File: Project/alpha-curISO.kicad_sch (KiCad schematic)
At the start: 43 parts, among them J2 SWD, U1 RP2040, U5 74AHCT1G125

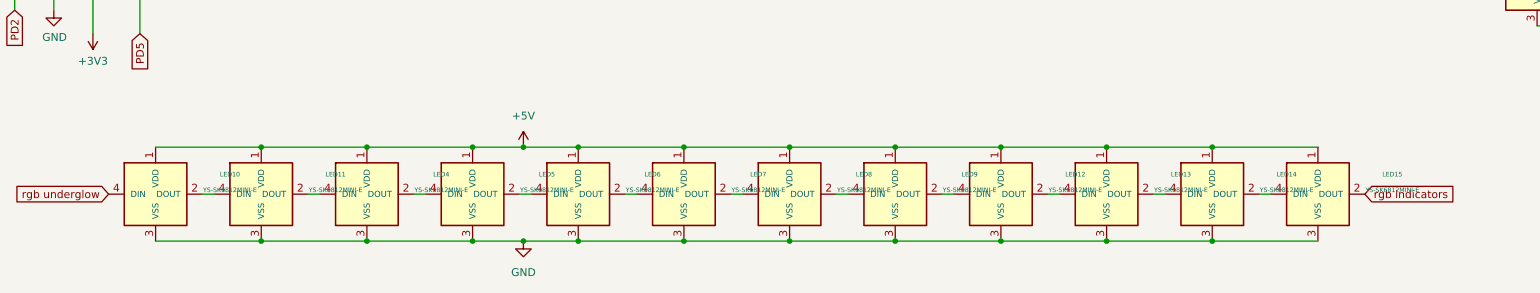
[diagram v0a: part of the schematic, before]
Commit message: added plate project for breakoff
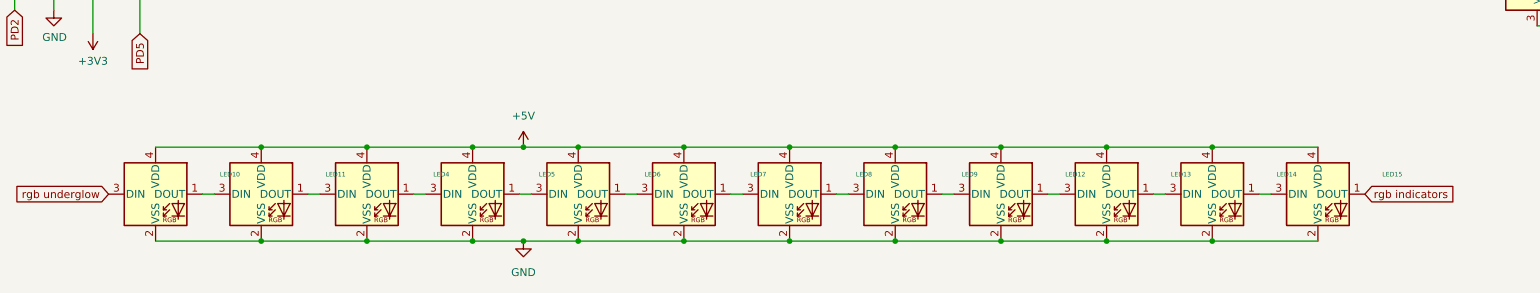
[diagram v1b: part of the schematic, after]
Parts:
- LED10, LED11, LED12, LED13, LED14, LED15, LED4, LED5, LED6, LED7, LED8, LED9: value YS-SK6812MINI-E -> WS2812_2020; footprint CrumpPrints:WS2812-2020 -> PCM_marbastlib-various:LED_WS2812_2020; symbol kbd:YS-SK6812MINI-E -> PCM_marbastlib-various:WS2812_2020
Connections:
- net +5V: now also LED10.4 (VDD), LED11.4 (VDD), LED12.4 (VDD), LED13.4 (VDD), LED14.4 (VDD), LED15.4 (VDD), LED4.4 (VDD), LED5.4 (VDD), LED6.4 (VDD), LED7.4 (VDD), LED8.4 (VDD), LED9.4 (VDD); no longer LED10.1 (VDD), LED11.1 (VDD), LED12.1 (VDD), LED13.1 (VDD), LED14.1 (VDD), LED15.1 (VDD), LED4.1 (VDD), LED5.1 (VDD), LED6.1 (VDD), LED7.1 (VDD), LED8.1 (VDD), LED9.1 (VDD)
- net GND: now also LED10.2 (VSS), LED11.2 (VSS), LED12.2 (VSS), LED13.2 (VSS), LED14.2 (VSS), LED15.2 (VSS), LED4.2 (VSS), LED5.2 (VSS), LED6.2 (VSS), LED7.2 (VSS), LED8.2 (VSS), LED9.2 (VSS); no longer LED10.3 (VSS), LED11.3 (VSS), LED12.3 (VSS), LED13.3 (VSS), LED14.3 (VSS), LED15.3 (VSS), LED4.3 (VSS), LED5.3 (VSS), LED6.3 (VSS), LED7.3 (VSS), LED8.3 (VSS), LED9.3 (VSS)
- net rgb indicators: now also LED15.1 (DOUT); no longer LED15.2 (DOUT)
- net rgb underglow: now also LED10.3 (DIN); no longer LED10.4 (DIN)
- new net: LED13.1 (DOUT), LED14.3 (DIN)
- new net: LED12.1 (DOUT), LED13.3 (DIN)
- new net: LED5.1 (DOUT), LED6.3 (DIN)
- new net: LED4.1 (DOUT), LED5.3 (DIN)
- new net: LED11.1 (DOUT), LED4.3 (DIN)
- new net: LED12.3 (DIN), LED9.1 (DOUT)
- new net: LED8.1 (DOUT), LED9.3 (DIN)
- new net: LED6.1 (DOUT), LED7.3 (DIN)
- new net: LED7.1 (DOUT), LED8.3 (DIN)
- new net: LED10.1 (DOUT), LED11.3 (DIN)
- new net: LED14.1 (DOUT), LED15.3 (DIN)
